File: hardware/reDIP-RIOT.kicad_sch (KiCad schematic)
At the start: 31 parts, among them J1 Conn_01x20, J2 Conn_01x20, J3 Conn_02x05_Odd_Even, U1 NCP115AMX120TCG, U2 NCP115AMX330TCG, U3 SN74CBT16210CDGGR, U4 SN74CBT16210CDGGR, U5 74AHC1G14SE-7, U6 ICE5LP1K-SG48, U7 AT25EU0011A-SSHN-T

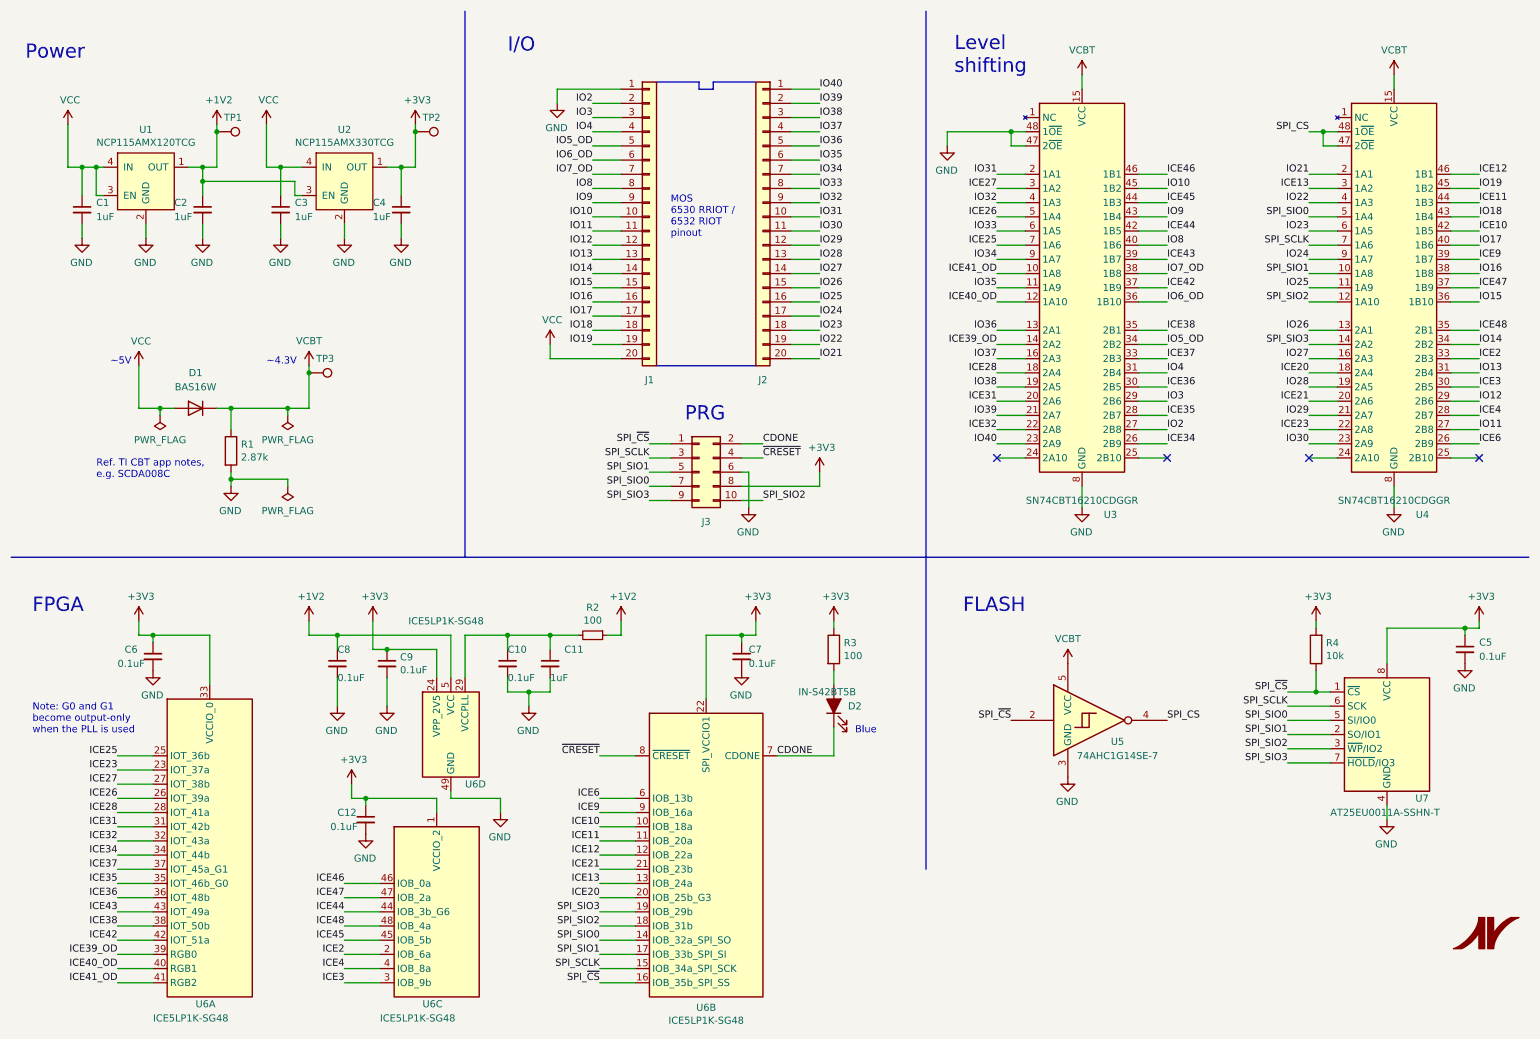
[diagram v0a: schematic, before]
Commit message: Added CRESET pull-up, removed CDONE LED
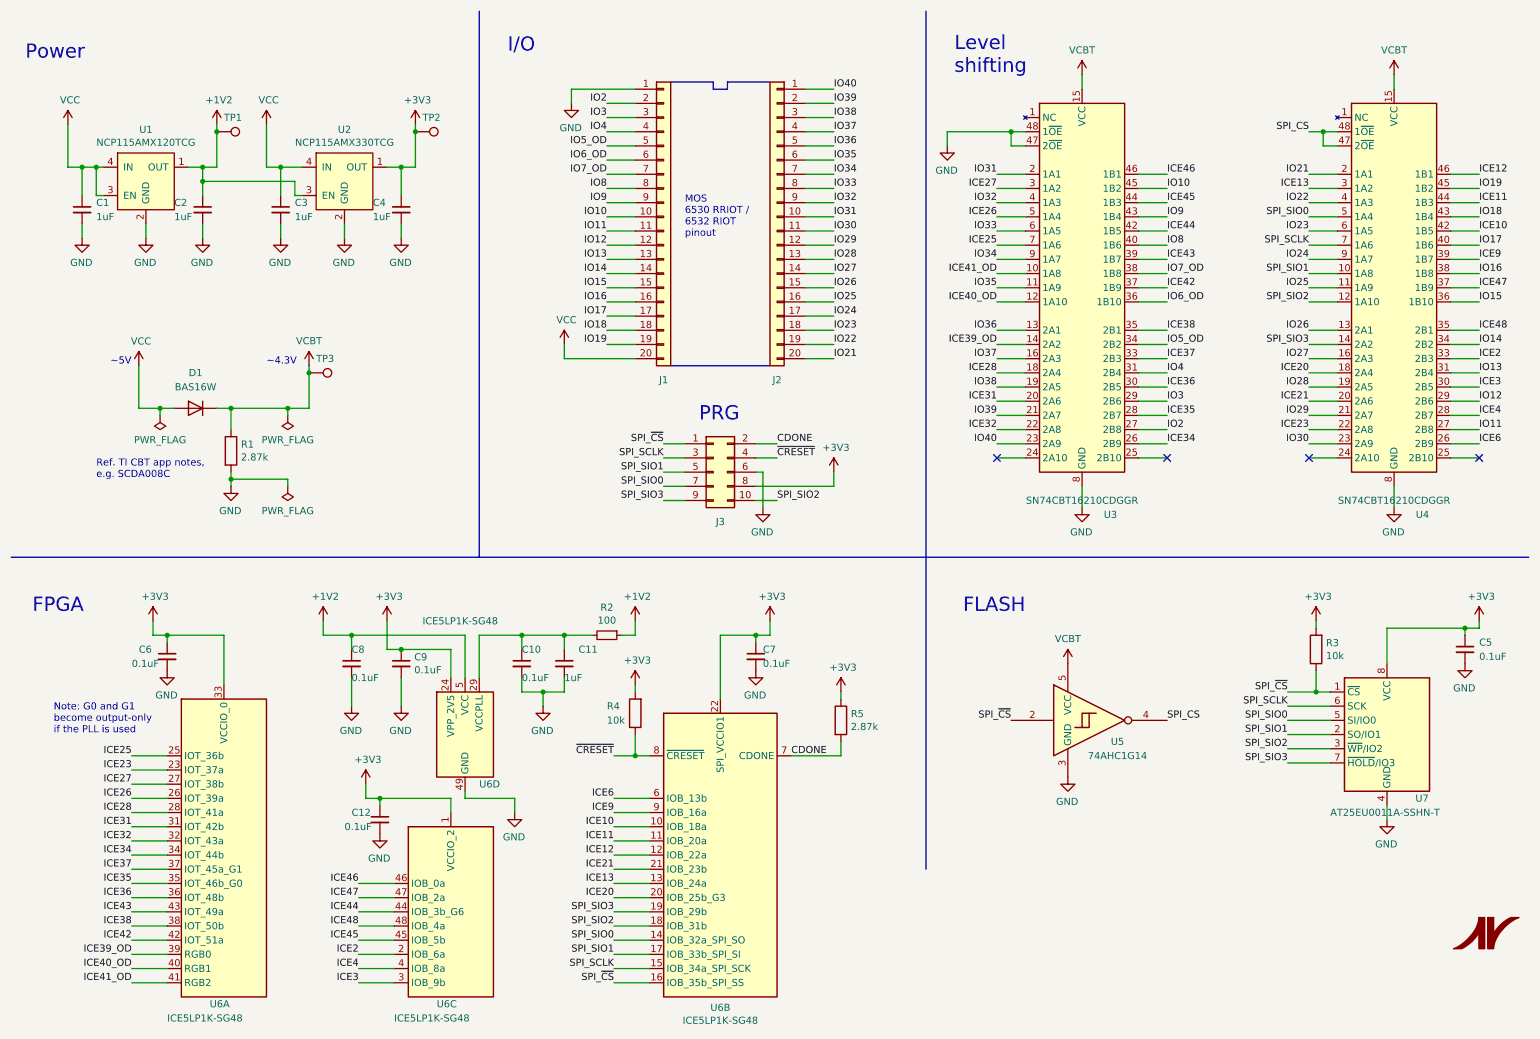
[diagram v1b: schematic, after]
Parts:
- removed D2: IN-S42BT5B, Inolux:LED_0402_1005Metric, symbol Device:LED_Filled
- removed R3: 100, Resistor_SMD:R_0201_0603Metric, symbol Device:R
- added R4: 10k, Resistor_SMD:R_0201_0603Metric, symbol Device:R
- added R5: 2.87k, Resistor_SMD:R_0201_0603Metric, symbol Device:R
- D1: Mfg onsemi -> Diodes; Notes (none) -> Replacement parts: BAS16W SOT-323/SC-70; PN BAS16WT1G -> BAS16W-7-F
- J3: now left out of the parts list
- U3, U4: Notes (none) -> Replacement parts: SN74CBT16210DGGR
- U5: value 74AHC1G14SE-7 -> 74AHC1G14; Notes (none) -> Replacement parts: 74AHC1G14 SOT-353/SC-70-5
- U7: Notes (none) -> Replacement parts: 1MBit SPI flash SOIC-8
- renumbered R4 to R3
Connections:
- net +3V3: now also R4.2, R5.1
- net CDONE: now also R5.2
- net ~{CRESET}: now also R4.1
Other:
- note added: "Note: G0 and G1 become output-only if the PLL is used"
- note removed: "Blue"
- note removed: "Note: G0 and G1 become output-only when the PLL is used"
- moved on the sheet: C10, C11, C12, C6, C7, C8, C9, J1, J2, J3, R2, U6A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

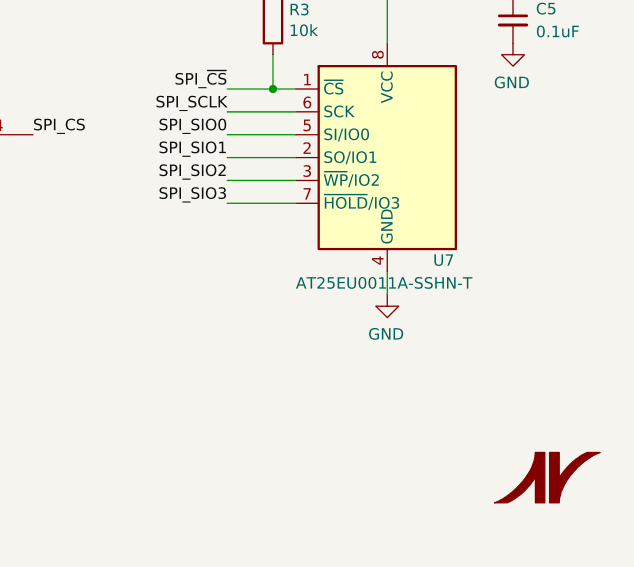
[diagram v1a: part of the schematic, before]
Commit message: Cleanup
* Removed unused footprints
* Rounded rectangle pads for SOT footprints
* Increased drill to 0.8mm for header pins
* Corrected BOM text
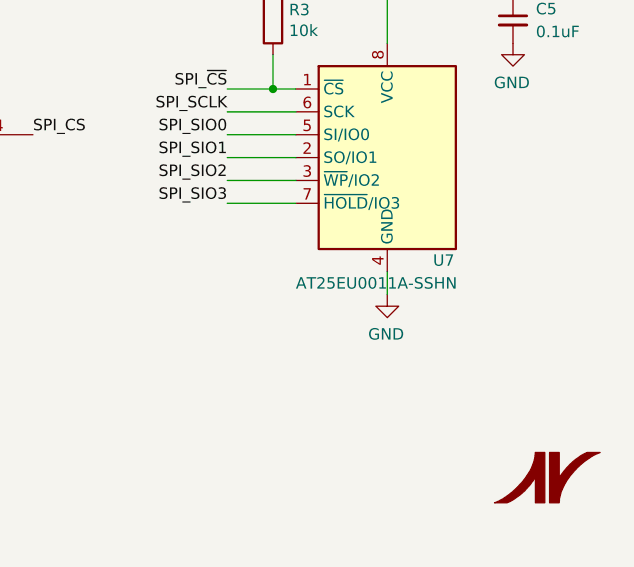
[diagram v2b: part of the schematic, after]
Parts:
- D1: footprint Package_TO_SOT_SMD:SOT-323_SC-70 -> reDIP:SOT-323_SC-70
- U5: footprint Package_TO_SOT_SMD:SOT-353_SC-70-5 -> reDIP:SOT-353_SC-70-5
- U7: value AT25EU0011A-SSHN-T -> AT25EU0011A-SSHN; Notes Replacement parts: 1MBit SPI flash SOIC-8 -> Replacement parts: 1MBit SPI flash SOIC-8/SOP-8
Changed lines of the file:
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@@
       (effects (font (size 1.27 1.27)) hide)
     )
-    (property "Description" "IC BUS SWITCH TVSOP-56" (at 260.35 62.23 0)
+    (property "Description" "IC BUS SWITCH TSSOP-48" (at 260.35 62.23 0)
       (effects (font (size 1.27 1.27)) hide)
     )
@@
       (effects (font (size 1.27 1.27)))
     )
-    (property "Footprint" "Package_TO_SOT_SMD:SOT-323_SC-70" (at 45.72 88.265 0)
+    (property "Footprint" "reDIP:SOT-323_SC-70" (at 45.72 88.265 0)
       (effects (font (size 1.27 1.27)) hide)
     )
@@
       (effects (font (size 1.27 1.27)) hide)
     )
-    (property "Description" "IC BUS SWITCH TVSOP-56" (at 204.47 62.23 0)
+    (property "Description" "IC BUS SWITCH TSSOP-48" (at 204.47 62.23 0)
       (effects (font (size 1.27 1.27)) hide)
     )
@@
       (effects (font (size 1.27 1.27)) (justify left))
     )
-    (property "Value" "AT25EU0011A-SSHN-T" (at 248.92 156.21 0)
+    (property "Value" "AT25EU0011A-SSHN" (at 248.92 156.21 0)
       (effects (font (size 1.27 1.27)) (justify left))
     )
@@
       (effects (font (size 1.27 1.27)) hide)
     )
-    (property "Notes" "Replacement parts: 1MBit SPI flash SOIC-8" (at 259.08 142.24 0)
+    (property "Notes" "Replacement parts: 1MBit SPI flash SOIC-8/SOP-8" (at 259.08 142.24 0)
       (effects (font (size 1.27 1.27)) hide)
     )
@@
       (effects (font (size 1.27 1.27)))
     )
-    (property "Footprint" "Package_TO_SOT_SMD:SOT-353_SC-70-5" (at 207.01 139.7 0)
-      (effects (font (size 1.27 1.27)) hide)
-    )
+    (property "Footprint" "reDIP:SOT-353_SC-70-5" (at 207.01 139.7 0)
+      (effects (font (size 1.27 1.27)) hide)
+    )

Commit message: Added example pin headers to BOM
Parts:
- J1, J2: Mfg (none) -> XKB; Notes (none) -> Replacement parts: XKB X5511WV-20-C396D43-1220, other simil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; PN (none) -> X5511WV-20-C35D35-1000
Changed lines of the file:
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@@
       (effects (font (size 1.27 1.27)) hide)
     )
-    (property "Datasheet" "~" (at 129.54 49.53 0)
-      (effects (font (size 1.27 1.27)) hide)
-    )
-    (property "Mfg" "" (at 129.54 49.53 0)
-      (effects (font (size 1.27 1.27)) hide)
-    )
-    (property "PN" "" (at 129.54 49.53 0)
-      (effects (font (size 1.27 1.27)) hide)
-    )
-    (property "Description" "CONN HDR ROUND PIN 0.5mm 20 POS .100\" GOLD MATING 3.5mm TAIL 3mm" (at 129.54 49.53 0)
+    (property "Datasheet" "https://www.helloxkb.com/Home/Goods/goodsInfo/id/72370.html" (at 129.54 49.53 0)
+      (effects (font (size 1.27 1.27)) hide)
+    )
+    (property "Mfg" "XKB" (at 129.54 49.53 0)
+      (effects (font (size 1.27 1.27)) hide)
+    )
+    (property "PN" "X5511WV-20-C35D35-1000" (at 129.54 49.53 0)
+      (effects (font (size 1.27 1.27)) hide)
+    )
+    (property "Description" "CONN HDR CIRCULAR PIN 0.5mm 20 POS .100\" GOLD MATING 3mm TAIL 3mm" (at 129.54 49.53 0)
+      (effects (font (size 1.27 1.27)) hide)
+    )
+    (property "Notes" "Replacement parts: XKB X5511WV-20-C396D43-1220, other similar hdr circular pin ~0.5mm" (at 129.54 49.53 0)
       (effects (font (size 1.27 1.27)) hide)
     )
@@
       (effects (font (size 1.27 1.27)) hide)
     )
-    (property "Datasheet" "~" (at 149.86 49.53 0)
-      (effects (font (size 1.27 1.27)) hide)
-    )
-    (property "Description" "CONN HDR ROUND PIN 0.5mm 20 POS .100\" GOLD MATING 3.5mm TAIL 3mm" (at 149.86 49.53 0)
-      (effects (font (size 1.27 1.27)) hide)
-    )
-    (property "Mfg" "" (at 149.86 49.53 0)
-      (effects (font (size 1.27 1.27)) hide)
-    )
-    (property "PN" "" (at 149.86 49.53 0)
-      (effects (font (size 1.27 1.27)) hide)
-    )
+    (property "Datasheet" "https://www.helloxkb.com/Home/Goods/goodsInfo/id/72370.html" (at 149.86 49.53 0)
+      (effects (font (size 1.27 1.27)) hide)
+    )
+    (property "Description" "CONN HDR CIRCULAR PIN 0.5mm 20 POS .100\" GOLD MATING 3mm TAIL 3mm" (at 149.86 49.53 0)
+      (effects (font (size 1.27 1.27)) hide)
+    )
+    (property "Mfg" "XKB" (at 149.86 49.53 0)
+      (effects (font (size 1.27 1.27)) hide)
+    )
+    (property "PN" "X5511WV-20-C35D35-1000" (at 149.86 49.53 0)
+      (effects (font (size 1.27 1.27)) hide)
+    )
+    (property "Notes" "Replacement parts: XKB X5511WV-20-C396D43-1220, other similar hdr circular pin ~0.5mm" (at 149.86 49.53 0)
+      (effects (font (size 1.27 1.27)) hide)
+    )

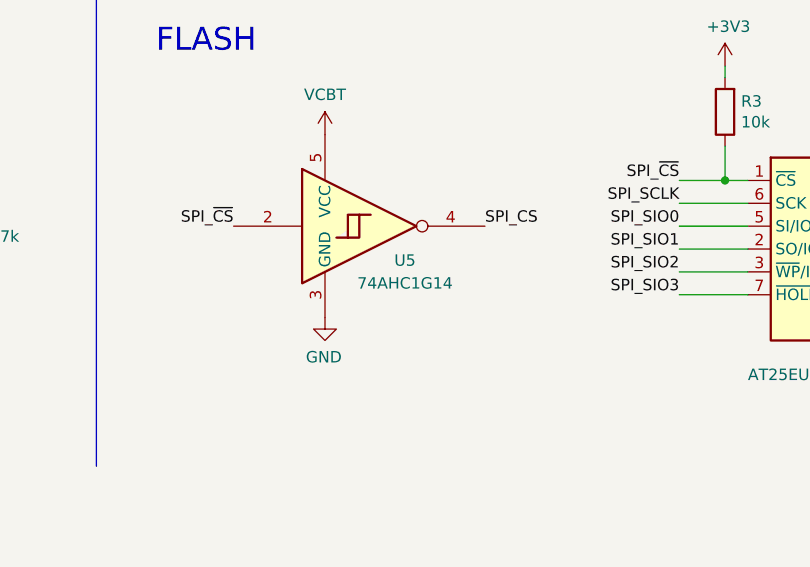
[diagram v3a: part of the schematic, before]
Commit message: Use 74AHCT1G14 for better signal level margins
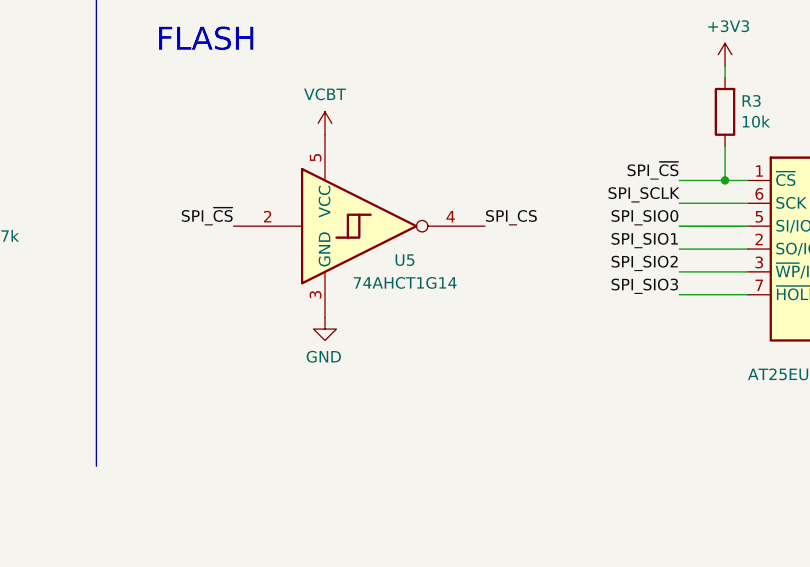
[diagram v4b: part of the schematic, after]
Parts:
- U5: value 74AHC1G14 -> 74AHCT1G14; symbol 74xGxx:74AHC1G14 -> 74xGxx:74AHCT1G14; Notes Replacement parts: 74AHC1G14 SOT-353/SC-70-5 -> Replacement parts: 74AHCT1G14 SOT-353/SC-70-5; PN 74AHC1G14SE-7 -> 74AHCT1G14SE-7
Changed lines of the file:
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@@
     )
   )
-  (symbol (lib_id "74xGxx:74AHC1G14") (at 207.01 139.7 0) (unit 1)
+  (symbol (lib_id "74xGxx:74AHCT1G14") (at 207.01 139.7 0) (unit 1)
     (in_bom yes) (on_board yes) (dnp no)
     (property "Reference" "U5" (at 210.82 143.51 0)
       (effects (font (size 1.27 1.27)))
     )
-    (property "Value" "74AHC1G14" (at 210.82 146.05 0)
+    (property "Value" "74AHCT1G14" (at 210.82 146.05 0)
       (effects (font (size 1.27 1.27)))
     )
@@
       (effects (font (size 1.27 1.27)) hide)
     )
-    (property "Datasheet" "https://www.diodes.com/assets/Datasheets/74AHC1G14.pdf" (at 207.01 139.7 0)
+    (property "Datasheet" "https://www.diodes.com/assets/Datasheets/74AHCT1G14.pdf" (at 207.01 139.7 0)
       (effects (font (size 1.27 1.27)) hide)
     )
@@
       (effects (font (size 1.27 1.27)) hide)
     )
-    (property "PN" "74AHC1G14SE-7" (at 207.01 139.7 0)
+    (property "PN" "74AHCT1G14SE-7" (at 207.01 139.7 0)
       (effects (font (size 1.27 1.27)) hide)
     )
-    (property "Notes" "Replacement parts: 74AHC1G14 SOT-353/SC-70-5" (at 207.01 139.7 0)
+    (property "Notes" "Replacement parts: 74AHCT1G14 SOT-353/SC-70-5" (at 207.01 139.7 0)
       (effects (font (size 1.27 1.27)) hide)
     )

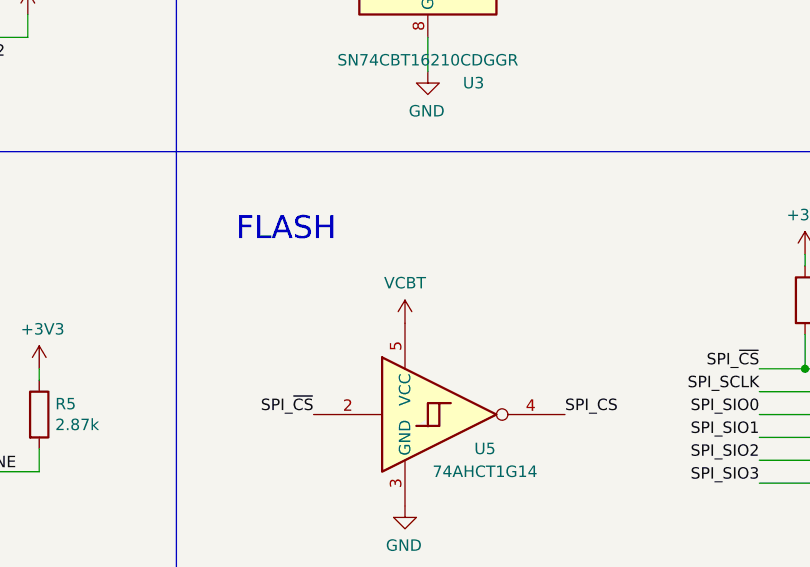
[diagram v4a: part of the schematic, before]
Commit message: Power supply for 74AHCT1G14 within range
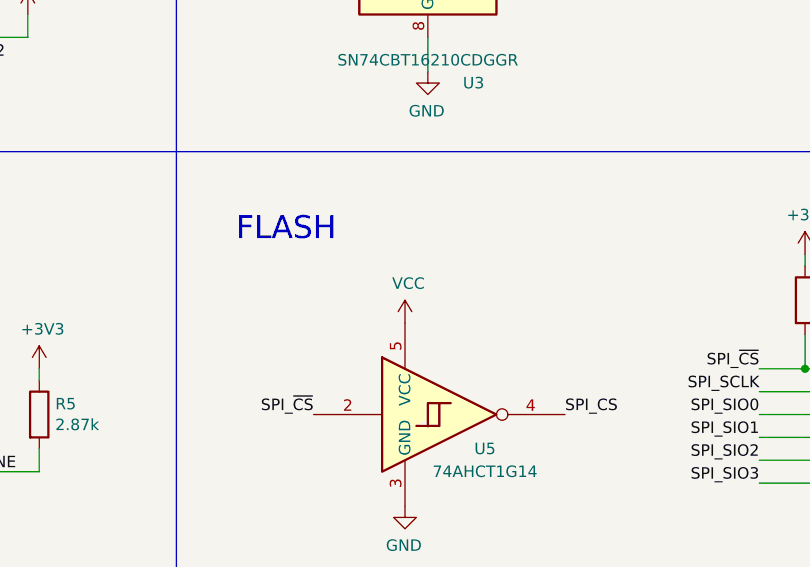
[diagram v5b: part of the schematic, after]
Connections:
- net VCBT: no longer U5.5 (VCC)
- net VCC: now also U5.5 (VCC)
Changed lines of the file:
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@@
-    )
-  )
-  (symbol (lib_id "reDIP:VCBT") (at 201.93 129.54 0) (unit 1)
-    (in_bom yes) (on_board yes) (dnp no)
-    (property "Reference" "#PWR030" (at 201.93 133.35 0)
-      (effects (font (size 1.27 1.27)) hide)
-    )
-    (property "Value" "VCBT" (at 201.93 125.095 0)
-      (effects (font (size 1.27 1.27)))
-    )
-    (property "Footprint" "" (at 201.93 129.54 0)
-      (effects (font (size 1.27 1.27)) hide)
-    )
-    (property "Datasheet" "" (at 201.93 129.54 0)
-      (effects (font (size 1.27 1.27)) hide)
-    )
-    (pin "1")
-    (instances
-      (project "reDIP-RIOT"
-        (path "/34d03349-6d78-4165-a683-2d8b76f2bae8"
-          (reference "#PWR030") (unit 1)
-        )
-      )
     )
   )
@@
         )
       )
+    )
+  )
+  (symbol (lib_id "power:VCC") (at 201.93 129.54 0) (unit 1)
+    (in_bom yes) (on_board yes) (dnp no)
+    (property "Reference" "#PWR044" (at 201.93 133.35 0)
+      (effects (font (size 1.27 1.27)) hide)
+    )
+    (property "Value" "VCC" (at 202.311 125.1458 0)
+      (effects (font (size 1.27 1.27)))
+    )
+    (property "Footprint" "" (at 201.93 129.54 0)
+      (effects (font (size 1.27 1.27)) hide)
+    )
+    (property "Datasheet" "" (at 201.93 129.54 0)
+      (effects (font (size 1.27 1.27)) hide)
+    )
+    (pin "1")
+    (instances
+      (project "reDIP-RIOT"
+        (path "/34d03349-6d78-4165-a683-2d8b76f2bae8"
+          (reference "#PWR044") (unit 1)
+        )
+      )
